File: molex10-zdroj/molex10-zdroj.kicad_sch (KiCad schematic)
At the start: 9 parts, among them J1 Conn_01x04, J2 Conn_02x04_Counter_Clockwise, J3 Conn_01x04, J4 Conn_01x02, J5 Conn_01x02

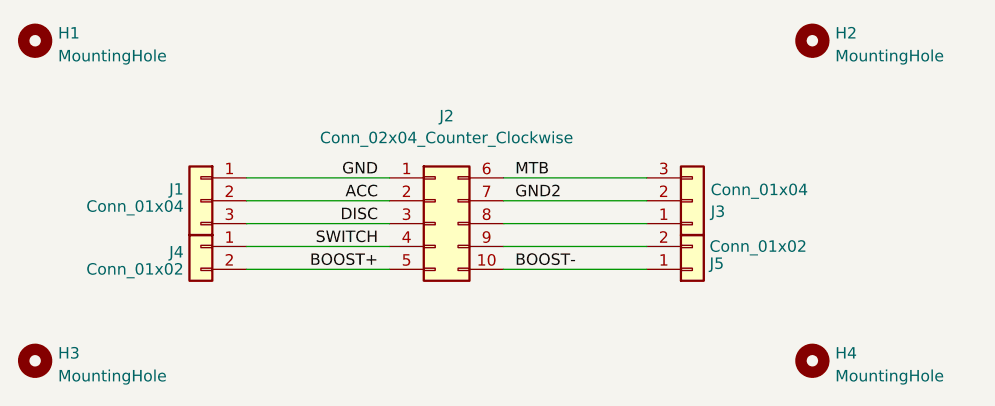
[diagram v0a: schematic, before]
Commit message: Use screw terminal symbols, use MVE25-5-V as values.
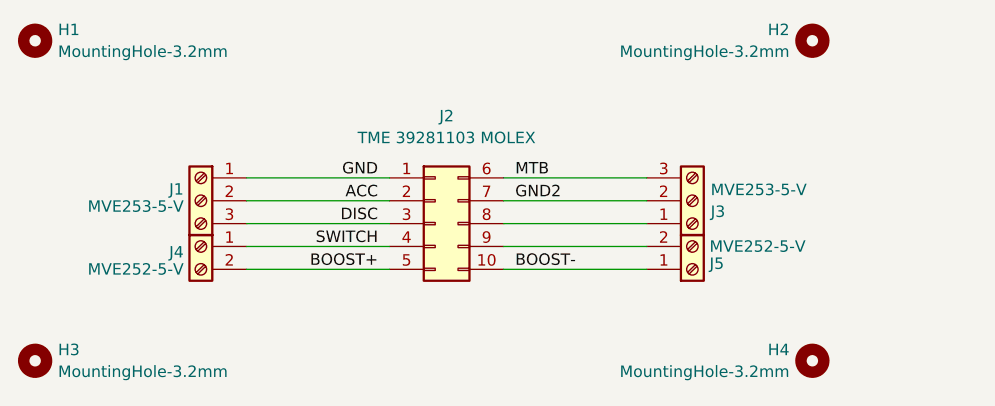
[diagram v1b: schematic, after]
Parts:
- H1, H2, H3, H4: value MountingHole -> MountingHole-3.2mm
- J1, J3: value Conn_01x04 -> MVE253-5-V; symbol Connector_Generic:Conn_01x03 -> Connector:Screw_Terminal_01x03
- J2: value Conn_02x04_Counter_Clockwise -> TME 39281103 MOLEX
- J4, J5: value Conn_01x02 -> MVE252-5-V; symbol Connector_Generic:Conn_01x02 -> Connector:Screw_Terminal_01x02
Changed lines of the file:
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@@
       (effects (font (size 1.27 1.27)))
     )
-    (property "Value" "Conn_02x04_Counter_Clockwise" (at 105.41 51.435 0)
+    (property "Value" "TME 39281103 MOLEX" (at 105.41 51.435 0)
       (effects (font (size 1.27 1.27)))
     )
@@
     )
   )
-  (symbol (lib_id "Connector_Generic:Conn_01x03") (at 132.715 58.42 0) (mirror x) (unit 1)
+  (symbol (lib_id "Connector:Screw_Terminal_01x03") (at 132.715 58.42 0) (mirror x) (unit 1)
     (in_bom yes) (on_board yes) (dnp no)
     (property "Reference" "J3" (at 134.747 59.6321 0)
       (effects (font (size 1.27 1.27)) (justify left))
     )
-    (property "Value" "Conn_01x04" (at 134.747 57.2079 0)
+    (property "Value" "MVE253-5-V" (at 134.747 57.2079 0)
       (effects (font (size 1.27 1.27)) (justify left))
     )
@@
   (symbol (lib_id "Mechanical:MountingHole") (at 59.69 40.64 0) (unit 1)
     (in_bom yes) (on_board yes) (dnp no) (fields_autoplaced)
-    (property "Reference" "H1" (at 62.23 39.8053 0)
-      (effects (font (size 1.27 1.27)) (justify left))
-    )
-    (property "Value" "MountingHole" (at 62.23 42.3422 0)
+    (property "Reference" "H1" (at 62.23 39.4279 0)
+      (effects (font (size 1.27 1.27)) (justify left))
+    )
+    (property "Value" "MountingHole-3.2mm" (at 62.23 41.8521 0)
       (effects (font (size 1.27 1.27)) (justify left))
     )
@@
     )
   )
-  (symbol (lib_id "Connector_Generic:Conn_01x03") (at 78.105 58.42 0) (mirror y) (unit 1)
+  (symbol (lib_id "Connector:Screw_Terminal_01x03") (at 78.105 58.42 0) (mirror y) (unit 1)
     (in_bom yes) (on_board yes) (dnp no)
     (property "Reference" "J1" (at 76.2 57.15 0)
       (effects (font (size 1.27 1.27)) (justify left))
     )
-    (property "Value" "Conn_01x04" (at 76.2 59.055 0)
+    (property "Value" "MVE253-5-V" (at 76.2 59.055 0)
       (effects (font (size 1.27 1.27)) (justify left))
     )
@@
     )
   )
-  (symbol (lib_id "Connector_Generic:Conn_01x02") (at 78.105 63.5 0) (mirror y) (unit 1)
+  (symbol (lib_id "Connector:Screw_Terminal_01x02") (at 78.105 63.5 0) (mirror y) (unit 1)
     (in_bom yes) (on_board yes) (dnp no)
     (property "Reference" "J4" (at 76.2 64.135 0)
       (effects (font (size 1.27 1.27)) (justify left))
     )
-    (property "Value" "Conn_01x02" (at 76.2 66.04 0)
+    (property "Value" "MVE252-5-V" (at 76.2 66.04 0)
       (effects (font (size 1.27 1.27)) (justify left))
     )
@@
   (symbol (lib_id "Mechanical:MountingHole") (at 59.69 76.2 0) (unit 1)
     (in_bom yes) (on_board yes) (dnp no) (fields_autoplaced)
-    (property "Reference" "H3" (at 62.23 75.3653 0)
-      (effects (font (size 1.27 1.27)) (justify left))
-    )
-    (property "Value" "MountingHole" (at 62.23 77.9022 0)
+    (property "Reference" "H3" (at 62.23 74.9879 0)
+      (effects (font (size 1.27 1.27)) (justify left))
+    )
+    (property "Value" "MountingHole-3.2mm" (at 62.23 77.4121 0)
       (effects (font (size 1.27 1.27)) (justify left))
     )
@@
     )
   )
-  (symbol (lib_id "Mechanical:MountingHole") (at 146.05 76.2 0) (unit 1)
-    (in_bom yes) (on_board yes) (dnp no) (fields_autoplaced)
-    (property "Reference" "H4" (at 148.59 75.3653 0)
-      (effects (font (size 1.27 1.27)) (justify left))
-    )
-    (property "Value" "MountingHole" (at 148.59 77.9022 0)
+  (symbol (lib_id "Mechanical:MountingHole") (at 146.05 76.2 0) (mirror y) (unit 1)
+    (in_bom yes) (on_board yes) (dnp no)
+    (property "Reference" "H4" (at 143.51 74.9879 0)
+      (effects (font (size 1.27 1.27)) (justify left))
+    )
+    (property "Value" "MountingHole-3.2mm" (at 143.51 77.4121 0)
       (effects (font (size 1.27 1.27)) (justify left))
     )
@@
     )
   )
-  (symbol (lib_id "Connector_Generic:Conn_01x02") (at 132.715 66.04 0) (mirror x) (unit 1)
+  (symbol (lib_id "Connector:Screw_Terminal_01x02") (at 132.715 66.04 0) (mirror x) (unit 1)
     (in_bom yes) (on_board yes) (dnp no)
     (property "Reference" "J5" (at 134.62 65.405 0)
       (effects (font (size 1.27 1.27)) (justify left))
     )
-    (property "Value" "Conn_01x02" (at 134.62 63.5 0)
+    (property "Value" "MVE252-5-V" (at 134.62 63.5 0)
       (effects (font (size 1.27 1.27)) (justify left))
     )
@@
     )
   )
-  (symbol (lib_id "Mechanical:MountingHole") (at 146.05 40.64 0) (unit 1)
-    (in_bom yes) (on_board yes) (dnp no) (fields_autoplaced)
-    (property "Reference" "H2" (at 148.59 39.8053 0)
-      (effects (font (size 1.27 1.27)) (justify left))
-    )
-    (property "Value" "MountingHole" (at 148.59 42.3422 0)
-      (effects (font (size 1.27 1.27)) (justify left))
-    )
+  (symbol (lib_id "Mechanical:MountingHole") (at 146.05 40.64 0) (mirror y) (unit 1)
+    (in_bom yes) (on_board yes) (dnp no)
+    (property "Reference" "H2" (at 143.51 39.4279 0)
+      (effects (font (size 1.27 1.27)) (justify left))
+    )
+    (property "Value" "MountingHole-3.2mm" (at 143.51 41.8521 0)
+      (effects (font (size 1.27 1.27)) (justify left))
+    )

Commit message: molex10-zdroj: flip MOLEX to bottom side.
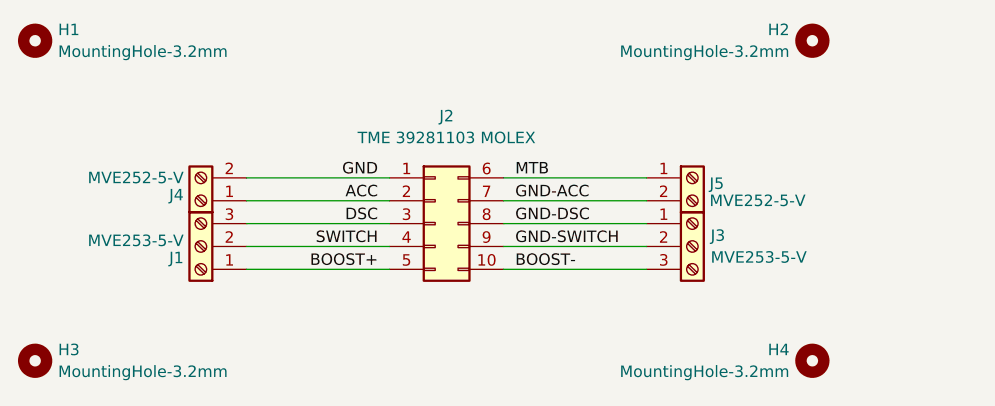
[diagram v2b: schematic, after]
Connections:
- net ACC: now also J4.1 (Pin_1); no longer J1.2 (Pin_2)
- net BOOST+: now also J1.1 (Pin_1); no longer J4.2 (Pin_2)
- net BOOST-: now also J3.3 (Pin_3); no longer J5.1 (Pin_1)
- net GND: now also J4.2 (Pin_2); no longer J1.1 (Pin_1)
- net MTB: now also J5.1 (Pin_1); no longer J3.3 (Pin_3)
- net SWITCH: now also J1.2 (Pin_2); no longer J4.1 (Pin_1)
- net GND-DSC: now reaches J2.8 (Pin_8), J3.1 (Pin_1)
- net GND-ACC: now reaches J5.2 (Pin_2)
- net GND-ACC: now also J2.7 (Pin_7); no longer J2.9 (Pin_9)
- net DISC renamed DSC
- net GND2 renamed GND-SWITCH
- net GND-SWITCH: now also J2.9 (Pin_9); no longer J2.7 (Pin_7)
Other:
- moved on the sheet: J1, J3, J4, J5
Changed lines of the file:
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@@
+    (effects (font (size 1.27 1.27)) (justify left bottom))
+  )
+  (label "GND-SWITCH" (at 113.03 63.5 0) (fields_autoplaced)
     (effects (font (size 1.27 1.27)) (justify left bottom))
   )
@@
     (effects (font (size 1.27 1.27)) (justify right bottom))
   )
-  (label "GND2" (at 113.03 58.42 0) (fields_autoplaced)
-    (effects (font (size 1.27 1.27)) (justify left bottom))
-  )
-  (label "DISC" (at 97.79 60.96 180) (fields_autoplaced)
+  (label "GND-DSC" (at 113.03 60.96 0) (fields_autoplaced)
+    (effects (font (size 1.27 1.27)) (justify left bottom))
+  )
+  (label "GND-ACC" (at 113.03 58.42 0) (fields_autoplaced)
+    (effects (font (size 1.27 1.27)) (justify left bottom))
+  )
+  (label "DSC" (at 97.79 60.96 180) (fields_autoplaced)
     (effects (font (size 1.27 1.27)) (justify right bottom))
   )
@@
     )
   )
-  (symbol (lib_id "Connector:Screw_Terminal_01x03") (at 132.715 58.42 0) (mirror x) (unit 1)
-    (in_bom yes) (on_board yes) (dnp no)
-    (property "Reference" "J3" (at 134.747 59.6321 0)
-      (effects (font (size 1.27 1.27)) (justify left))
-    )
-    (property "Value" "MVE253-5-V" (at 134.747 57.2079 0)
-      (effects (font (size 1.27 1.27)) (justify left))
-    )
-    (property "Footprint" "TerminalBlock_Euroclamp:MVE253-5-V" (at 132.715 58.42 0)
-      (effects (font (size 1.27 1.27)) hide)
-    )
-    (property "Datasheet" "~" (at 132.715 58.42 0)
+  (symbol (lib_id "Connector:Screw_Terminal_01x03") (at 132.715 63.5 0) (unit 1)
+    (in_bom yes) (on_board yes) (dnp no)
+    (property "Reference" "J3" (at 134.747 62.2879 0)
+      (effects (font (size 1.27 1.27)) (justify left))
+    )
+    (property "Value" "MVE253-5-V" (at 134.747 64.7121 0)
+      (effects (font (size 1.27 1.27)) (justify left))
+    )
+    (property "Footprint" "TerminalBlock_Euroclamp:MVE253-5-V" (at 132.715 63.5 0)
+      (effects (font (size 1.27 1.27)) hide)
+    )
+    (property "Datasheet" "~" (at 132.715 63.5 0)
       (effects (font (size 1.27 1.27)) hide)
     )
@@
     )
   )
-  (symbol (lib_id "Connector:Screw_Terminal_01x03") (at 78.105 58.42 0) (mirror y) (unit 1)
-    (in_bom yes) (on_board yes) (dnp no)
-    (property "Reference" "J1" (at 76.2 57.15 0)
-      (effects (font (size 1.27 1.27)) (justify left))
-    )
-    (property "Value" "MVE253-5-V" (at 76.2 59.055 0)
-      (effects (font (size 1.27 1.27)) (justify left))
-    )
-    (property "Footprint" "TerminalBlock_Euroclamp:MVE253-5-V" (at 78.105 58.42 0)
+  (symbol (lib_id "Connector:Screw_Terminal_01x03") (at 78.105 63.5 180) (unit 1)
+    (in_bom yes) (on_board yes) (dnp no)
+    (property "Reference" "J1" (at 76.2 64.77 0)
+      (effects (font (size 1.27 1.27)) (justify left))
+    )
+    (property "Value" "MVE253-5-V" (at 76.2 62.865 0)
+      (effects (font (size 1.27 1.27)) (justify left))
+    )
+    (property "Footprint" "TerminalBlock_Euroclamp:MVE253-5-V" (at 78.105 63.5 0)
+      (effects (font (size 1.27 1.27)) hide)
+    )
+    (property "Datasheet" "~" (at 78.105 63.5 0)
+      (effects (font (size 1.27 1.27)) hide)
+    )
+    (pin "1")
+    (pin "2")
+    (pin "3")
+    (instances
+      (project "molex10-zdroj"
+        (path "/16aec8df-9fa9-47bc-9f05-f4ad438ebac2"
+          (reference "J1") (unit 1)
+        )
+      )
+    )
+  )
+  (symbol (lib_id "Connector:Screw_Terminal_01x02") (at 78.105 58.42 180) (unit 1)
+    (in_bom yes) (on_board yes) (dnp no)
+    (property "Reference" "J4" (at 76.2 57.785 0)
+      (effects (font (size 1.27 1.27)) (justify left))
+    )
+    (property "Value" "MVE252-5-V" (at 76.2 55.88 0)
+      (effects (font (size 1.27 1.27)) (justify left))
+    )
+    (property "Footprint" "TerminalBlock_Euroclamp:MVE252-5-V" (at 78.105 58.42 0)
       (effects (font (size 1.27 1.27)) hide)
     )
     (property "Datasheet" "~" (at 78.105 58.42 0)
-      (effects (font (size 1.27 1.27)) hide)
-    )
-    (pin "1")
-    (pin "2")
-    (pin "3")
-    (instances
-      (project "molex10-zdroj"
-        (path "/16aec8df-9fa9-47bc-9f05-f4ad438ebac2"
-          (reference "J1") (unit 1)
-        )
-      )
-    )
-  )
-  (symbol (lib_id "Connector:Screw_Terminal_01x02") (at 78.105 63.5 0) (mirror y) (unit 1)
-    (in_bom yes) (on_board yes) (dnp no)
-    (property "Reference" "J4" (at 76.2 64.135 0)
-      (effects (font (size 1.27 1.27)) (justify left))
-    )
-    (property "Value" "MVE252-5-V" (at 76.2 66.04 0)
-      (effects (font (size 1.27 1.27)) (justify left))
-    )
-    (property "Footprint" "TerminalBlock_Euroclamp:MVE252-5-V" (at 78.105 63.5 0)
-      (effects (font (size 1.27 1.27)) hide)
-    )
-    (property "Datasheet" "~" (at 78.105 63.5 0)
       (effects (font (size 1.27 1.27)) hide)
     )
@@
     )
   )
-  (symbol (lib_id "Connector:Screw_Terminal_01x02") (at 132.715 66.04 0) (mirror x) (unit 1)
-    (in_bom yes) (on_board yes) (dnp no)
-    (property "Reference" "J5" (at 134.62 65.405 0)
-      (effects (font (size 1.27 1.27)) (justify left))
-    )
-    (property "Value" "MVE252-5-V" (at 134.62 63.5 0)
-      (effects (font (size 1.27 1.27)) (justify left))
-    )
-    (property "Footprint" "TerminalBlock_Euroclamp:MVE252-5-V" (at 132.715 66.04 0)
-      (effects (font (size 1.27 1.27)) hide)
-    )
-    (property "Datasheet" "~" (at 132.715 66.04 0)
-      (effects (font (size 1.27 1.27)) hide)
-    )
+  (symbol (lib_id "Connector:Screw_Terminal_01x02") (at 132.715 55.88 0) (unit 1)
+    (in_bom yes) (on_board yes) (dnp no)
+    (property "Reference" "J5" (at 134.62 56.515 0)
+      (effects (font (size 1.27 1.27)) (justify left))
+    )
+    (property "Value" "MVE252-5-V" (at 134.62 58.42 0)
+      (effects (font (size 1.27 1.27)) (justify left))
+    )
+    (property "Footprint" "TerminalBlock_Euroclamp:MVE252-5-V" (at 132.715 55.88 0)
+      (effects (font (size 1.27 1.27)) hide)
+    )
+    (property "Datasheet" "~" (at 132.715 55.88 0)
+      (effects (font (size 1.27 1.27)) hide)
+    )
